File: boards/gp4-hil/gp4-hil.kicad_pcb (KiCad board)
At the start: 4 copper layers, 160 x 62 mm, 452 parts, among them J1 BEL_FUSE_0826-1G1T-23-F, J2 XILINX_JTAG, J3 XILINX_JTAG_ICESIDE, J4 XILINX_JTAG_ICESIDE, K1 CONN_3_PWROUT, P1 GPAK_ZIF, P2 2x10 HEADER, Q1 SSM6N58NU, Q11 SSM6N58NU, Q12 DMP2069UFY4, Q13 SSM6N58NU, Q14 SSM6N58NU, Q15 SSM6N58NU, Q16 SSM6N58NU, Q17 SSM6N58NU, Q18 SSM6N58NU, Q19 SSM6N58NU, Q20 SSM6N58NU, Q21 SSM6N58NU, Q22 DMP2069UFY4, U1 MIC2288-DFN, U10 AD9609, U11 DAC084S085, U12 DAC084S085, U13 DAC084S085, U14 DAC084S085, U15 TS3A4751, U16 TS3A4751, U17 TS3A4751, U18 TS3A4751, U19 TS3A4751, U2 XC7A100T-1FTG256C, U20 SIP32408, U21 SIP32408, U22 SIP32408, U23 SIP32408, U24 SIP32408, U25 TS3A4751, U26 TS3A4751, U27 TS3A4751, U28 TS3A4751, U29 TXB0104RUT, U3 LTC3374-QFN, U30 TXB0104RUT, U31 ADA4937-2, U32 SIP32408, U33 125 MHz, U34 INA199A2RSW, U35 INA199A2RSW, U36 INA199A2RSW, U4 SIP32408, U5 KSZ9031RN, U6 W25Q32FW, U7 25 MHz, U8 ADG726, U9 AD9609

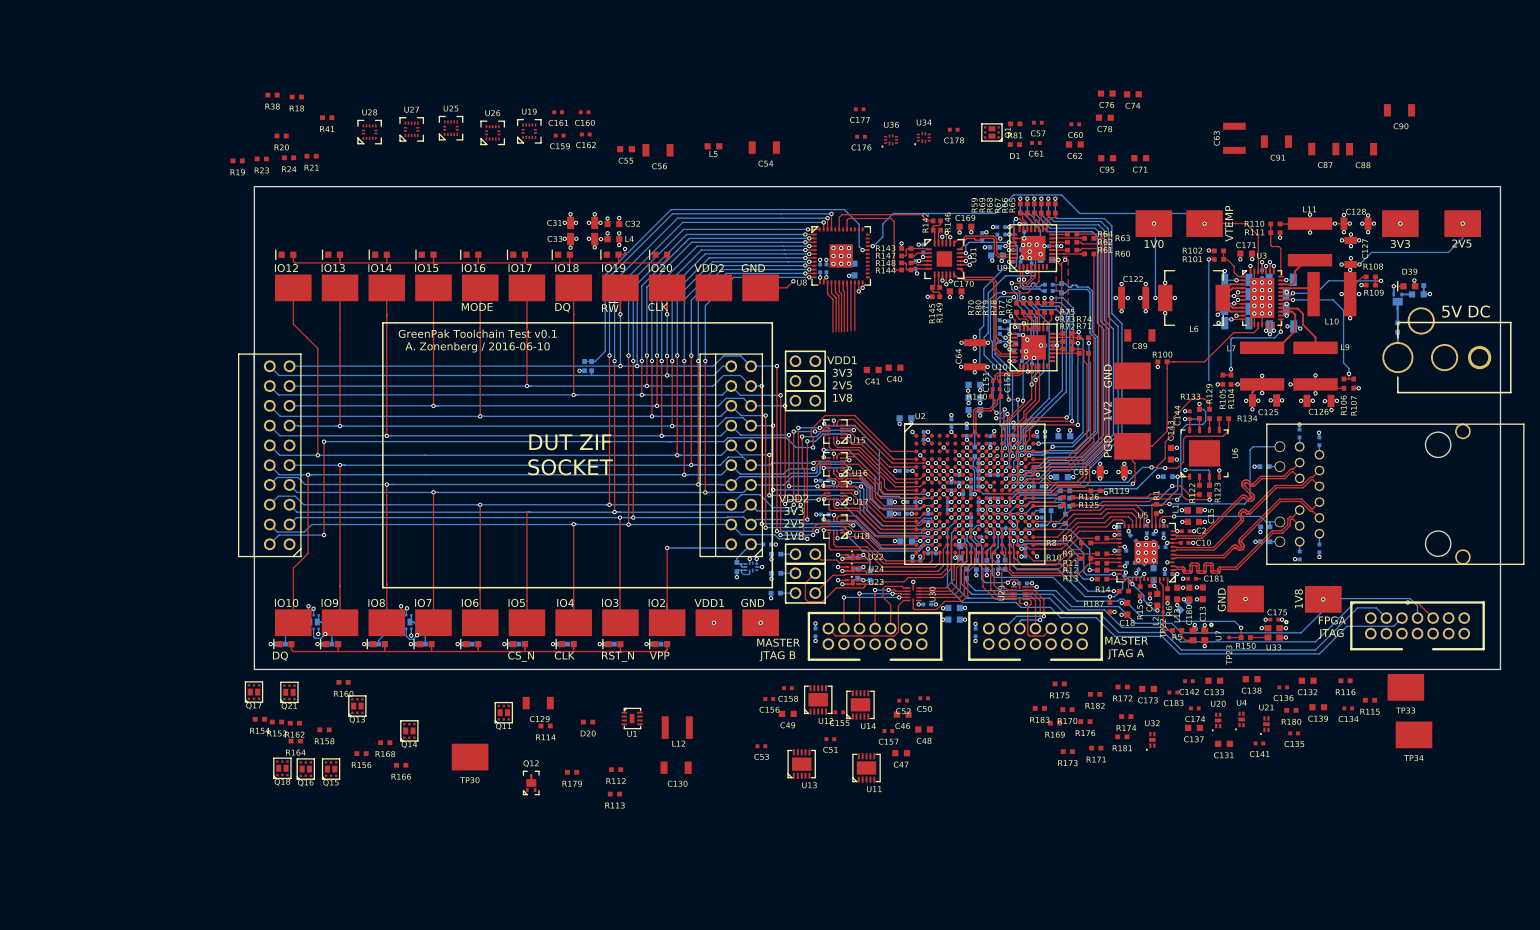
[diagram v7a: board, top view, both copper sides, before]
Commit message: Continued work on test board. Finally hooked up remote sense for 1V0.
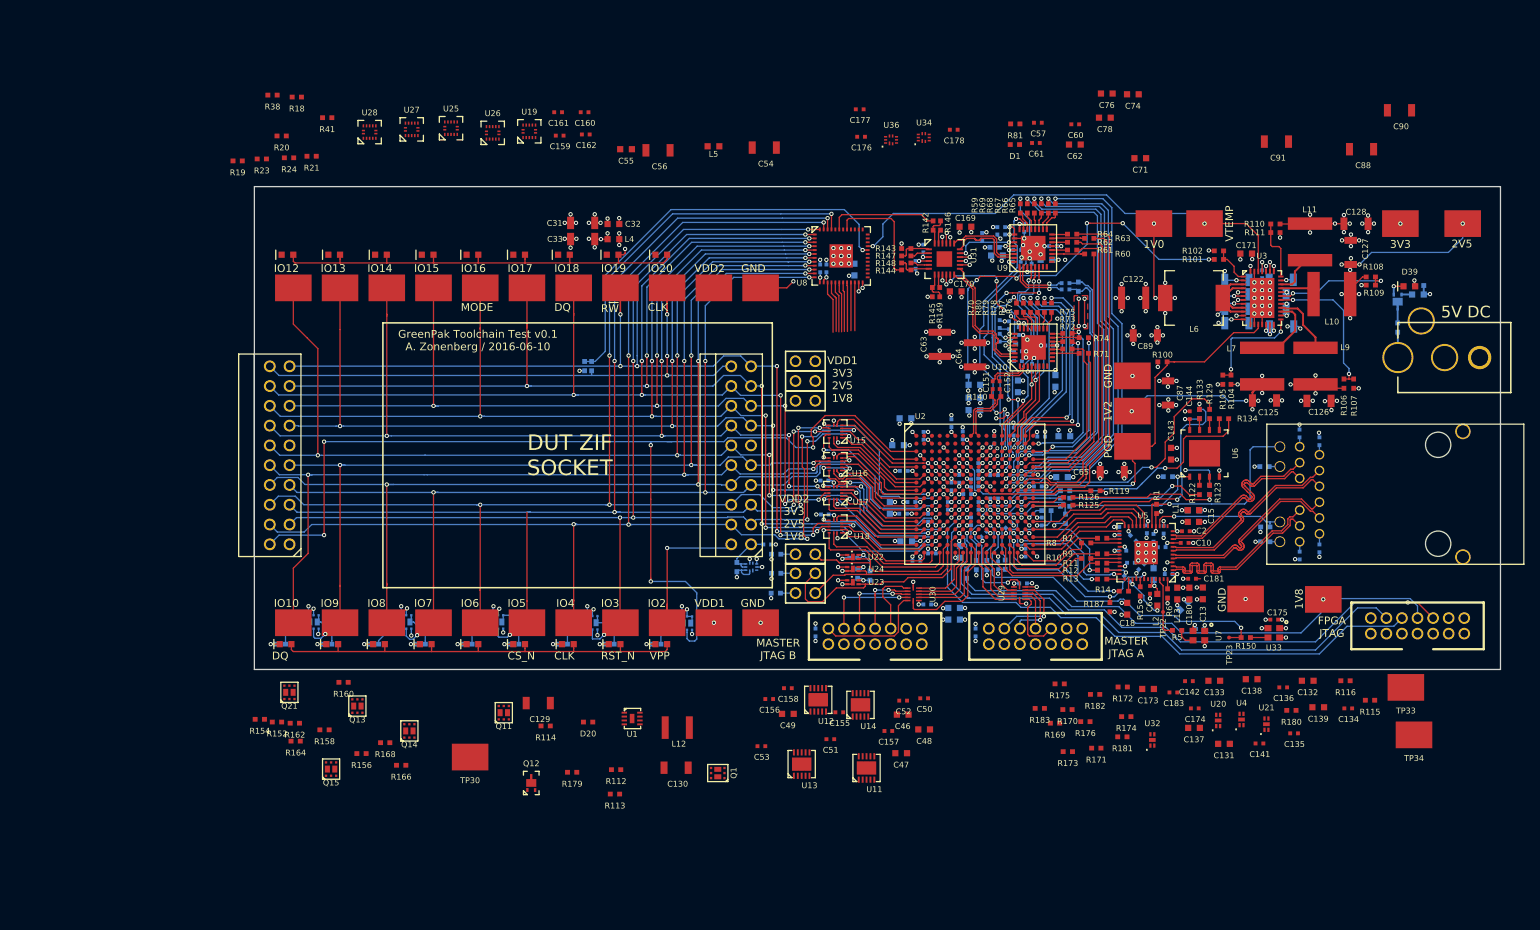
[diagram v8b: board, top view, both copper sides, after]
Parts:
- C40, C41, C95, Q16, Q17, Q18: moved to B.Cu
- moved Q1 89.5 mm to (80.5, 133.3)
- moved Q16 52.4 mm to (76.5, 114.0), turned to 180 degrees
- moved C63 46.2 mm to (109.0, 78.2), turned to 90 degrees
- moved C95 45.6 mm to (103.7, 91.2), turned to 180 degrees
- moved Q17 44.4 mm to (64.4, 114.0), turned to 180 degrees
- moved C87 37.2 mm to (138.3, 84.5), turned to 90 degrees
- moved Q18 33.5 mm to (52.3, 113.9), turned to 180 degrees
- moved C41 23.5 mm to (123.8, 83.0), turned to 270 degrees
- moved C40 16.0 mm to (119.0, 83.7), turned to 270 degrees
- moved R103 10.3 mm to (112.6, 81.8)
- moved C153 2.16 mm to (125.2, 71.2)
- moved C154 2.16 mm to (125.2, 70.4)
- moved R141 2.16 mm to (126.8, 70.8)
- moved C89 0.70 mm to (135.4, 77.1)
- moved C67 0.69 mm to (112.0, 90.0)
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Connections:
- Q1 pad D1: /Analog IO/DUT_GPIO2 -> Net-(Q1-PadD1)
- Q1 pad G1: /DUT/GPIO2_DIO -> /Analog IO/DUT_GPIO18
- Q13 pad G1: /Analog IO/DUT_GPIO2 -> /Analog IO/DUT_GPIO15
- Q14 pad G1: /Analog IO/DUT_GPIO3 -> /Analog IO/DUT_GPIO16
- Q15 pad G1: /Analog IO/DUT_GPIO4 -> /Analog IO/DUT_GPIO17
- Q16 pad D1: Net-(Q16-PadD1) -> /Analog IO/DUT_GPIO2
- Q16 pad G1: /Analog IO/DUT_GPIO5 -> /DUT/GPIO2_DIO
- Q16 pad G2: /Analog IO/DUT_GPIO15 -> /Analog IO/DUT_GPIO2
- Q17 pad G1: /Analog IO/DUT_GPIO6 -> /Analog IO/DUT_GPIO3
- Q17 pad G2: /Analog IO/DUT_GPIO16 -> /Analog IO/DUT_GPIO4
- Q18 pad G1: /Analog IO/DUT_GPIO18 -> /Analog IO/DUT_GPIO5
- Q18 pad G2: /Analog IO/DUT_GPIO17 -> /Analog IO/DUT_GPIO6
- R151 pad 1: Net-(Q13-PadD1) -> Net-(Q16-PadD2)
- R153 pad 1: Net-(Q14-PadD1) -> Net-(Q17-PadD1)
- R155 pad 1: Net-(Q15-PadD1) -> Net-(Q17-PadD2)
- R157 pad 1: Net-(Q16-PadD1) -> Net-(Q18-PadD1)
- R158 pad 1: Net-(Q16-PadD2) -> Net-(Q13-PadD1)
- R159 pad 1: Net-(Q17-PadD1) -> Net-(Q18-PadD2)
- R160 pad 1: Net-(Q17-PadD2) -> Net-(Q14-PadD1)
- R162 pad 1: Net-(Q18-PadD2) -> Net-(Q15-PadD1)
- R164 pad 1: Net-(Q18-PadD1) -> Net-(Q1-PadD1)
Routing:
- net /Analog IO/GND: track 1147.2 -> 1234.9 mm, vias 222 -> 243
- net /DUT/GPIO2_DIO: track 102.1 -> 135.2 mm, vias 3 -> 5
- net /Power supply/1V0_VSENSE: track 18.5 -> 49.1 mm, vias 1 -> 5
- net /Analog IO/2V5: track 244.9 -> 267.9 mm, vias 25 -> 34
- net /Analog IO/ADC_B_VCM: track 3.21 -> 19.9 mm, vias 2 -> 4
- net /Ethernet + JTAG/1V2: track 68.7 -> 84.5 mm, vias 14 -> 15
- net /FPGA support/1V0: track 126.5 -> 139.0 mm, vias 26 -> 30
- net /Analog IO/1V8: track 474.4 -> 483.4 mm, vias 56 -> 60
- net Net-(Q18-PadD1): track 0.00 -> 6.40 mm
- net Net-(Q16-PadD2): track 0.00 -> 6.27 mm
- net Net-(Q17-PadD2): track 0.00 -> 6.09 mm
- net Net-(Q17-PadD1): track 0.00 -> 5.86 mm
- net /Analog IO/DUT_GPIO2: track 20.4 -> 26.2 mm, vias 1 -> 2
- net /Analog IO/DUT_GPIO3: track 155.5 -> 161.2 mm, vias 7 -> 8
- net /Analog IO/DUT_GPIO5: track 158.3 -> 163.8 mm, vias 6 -> 7
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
